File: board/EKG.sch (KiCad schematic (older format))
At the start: 24 parts, among them U1 MAX86150EFF+T

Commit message: worked on schematics: - added new display - delete unwanted parts
Work on PCB:
- cleaned old pcb routes
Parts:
- removed C1, C2: 10pF, Capacitor_SMD:C_0201_0603Metric, symbol Device:C
- removed C3, C7: 22µF, Capacitor_SMD:C_0603_1608Metric, symbol Device:C
- removed C4, C6: 100nF, Capacitor_SMD:C_0201_0603Metric, symbol Device:C
- removed C5, C8: 1µF, Capacitor_SMD:C_0402_1005Metric, symbol Device:C
- removed R1, R2, R3, R8: 0, Resistor_SMD:R_0201_0603Metric, symbol Device:R
- removed R4, R7: DNP, Resistor_SMD:R_0201_0603Metric, symbol Device:R
- removed R5, R6, R9: 49.9k, Resistor_SMD:R_0201_0603Metric, symbol Device:R
- removed TP1: ECG_N, TestPoint:TestPoint_THTPad_D2.0mm_Drill1.0mm, symbol Connector:TestPoint
- removed TP2: ECG_P, TestPoint:TestPoint_THTPad_D2.0mm_Drill1.0mm, symbol Connector:TestPoint
- removed U1: MAX86150EFF+T, maxim:MAX86150, symbol MAX86150:MAX86150EFF+T
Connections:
- no-connect marks 8 -> 0

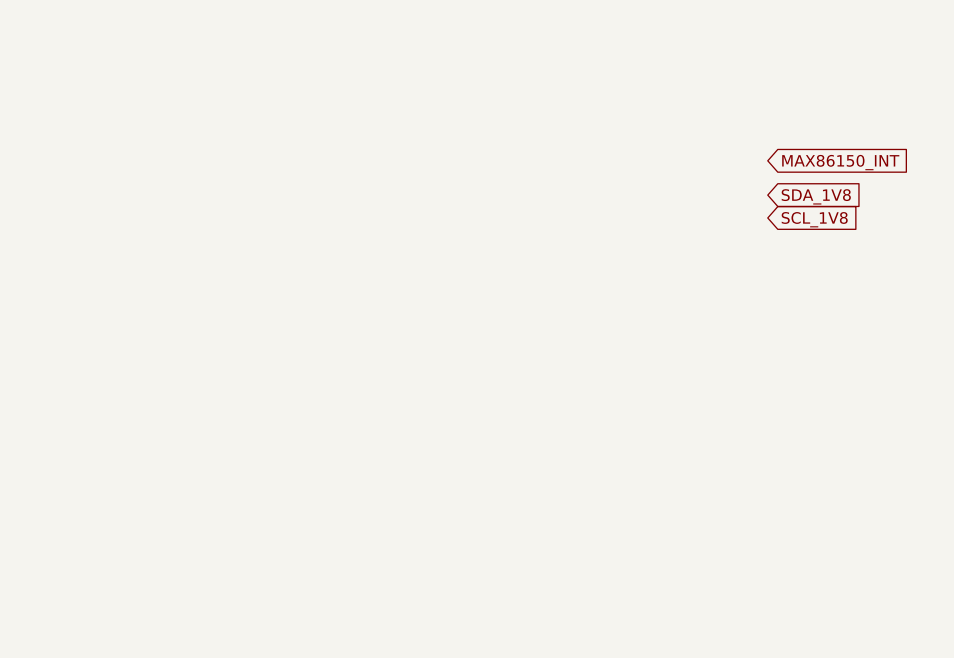
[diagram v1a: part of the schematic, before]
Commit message: - Added connector lib - added footprint for schottkey diode - added keep-out for new display
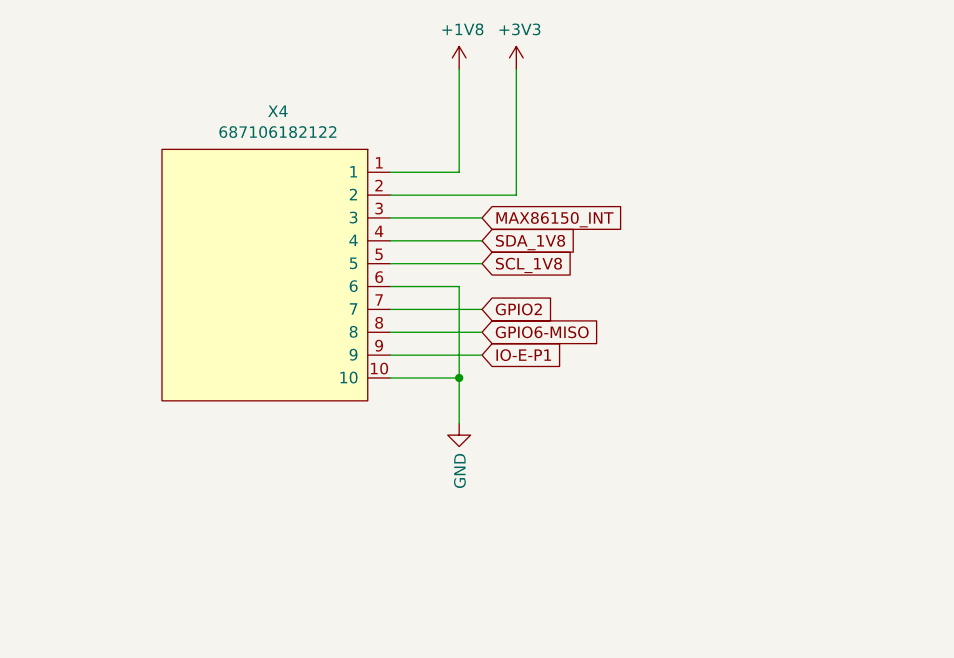
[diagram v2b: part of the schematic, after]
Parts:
- added X4: 687106182122, WR-FPC 0.50 mm SMT ZIF Horizontal Dual Contact:687110182122, symbol 687106182122:687106182122
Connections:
- net MAX86150_INT: now also X4.3
- net SCL_1V8: now also X4.5
- net SDA_1V8: now also X4.4
- new net +1V8: X4.1
- new net +3V3: X4.2
- new net GND: X4.10, X4.6
- new net GPIO2: X4.7
- new net GPIO6-MISO: X4.8
- new net IO-E-P1: X4.9
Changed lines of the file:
@@
 Comment4 ""
 $EndDescr
-Text GLabel 7800 3650 2    50   Input ~ 0
+Text GLabel 6550 3850 2    50   Input ~ 0
 SDA_1V8
-Text GLabel 7800 3750 2    50   Input ~ 0
+Text GLabel 6550 3950 2    50   Input ~ 0
 SCL_1V8
-Text GLabel 7800 3500 2    50   Input ~ 0
+Text GLabel 6550 3750 2    50   Input ~ 0
 MAX86150_INT
 $Comp
@@
 	-1   0    0    1
 $EndComp
+$Comp
+L power:+1V8 #PWR?
+U 1 1 610C6323
+P 6450 3100
+AR Path="/5CB104E6/610C6323" Ref="#PWR?"  Part="1"
+AR Path="/5CB104CE/610C6323" Ref="#PWR0115"  Part="1"
+F 0 "#PWR0115" H 6450 2950 50  0001 C CNN
+F 1 "+1V8" H 6465 3273 50  0000 C CNN
+F 2 "" H 6450 3100 50  0001 C CNN
+F 3 "" H 6450 3100 50  0001 C CNN
+	1    6450 3100
+	1    0    0    -1
+$EndComp
+$Comp
+L power:+3V3 #PWR?
+U 1 1 610C6329
+P 6700 3100
+AR Path="/5CB104E6/610C6329" Ref="#PWR?"  Part="1"
+AR Path="/5CB104CE/610C6329" Ref="#PWR0116"  Part="1"
+F 0 "#PWR0116" H 6700 2950 50  0001 C CNN
+F 1 "+3V3" H 6715 3273 50  0000 C CNN
+F 2 "" H 6700 3100 50  0001 C CNN
+F 3 "" H 6700 3100 50  0001 C CNN
+	1    6700 3100
+	1    0    0    -1
+$EndComp
+$Comp
+L power:GND #PWR?
+U 1 1 610C6FD9
+P 6450 4650
+AR Path="/5CB104E6/610C6FD9" Ref="#PWR?"  Part="1"
+AR Path="/5CB104CE/610C6FD9" Ref="#PWR0117"  Part="1"
+F 0 "#PWR0117" H 6450 4400 50  0001 C CNN
+F 1 "GND" V 6455 4522 50  0000 R CNN
+F 2 "" H 6450 4650 50  0001 C CNN
+F 3 "" H 6450 4650 50  0001 C CNN
+	1    6450 4650
+	1    0    0    -1
+$EndComp
+Text GLabel 6550 4350 2    50   Input ~ 0
+IO-E-P1
+Text GLabel 6550 4250 2    50   Input ~ 0
+GPIO6-MISO
+Text GLabel 6550 4150 2    50   Input ~ 0
+GPIO2
+$Comp
+L 687106182122:687106182122 X4
+U 1 1 610D31AF
+P 5600 4000
+F 0 "X4" H 5658 4715 50  0000 C CNN
+F 1 "687106182122" H 5658 4624 50  0000 C CNN
+F 2 "WR-FPC 0.50 mm SMT ZIF Horizontal Dual Contact:687110182122" H 5900 4550 50  0001 C CNN
+F 3 "" H 5900 4550 50  0001 C CNN
+	1    5600 4000
+	1    0    0    -1
+$EndComp
+Wire Wire Line
+	6450 3550 6150 3550
+Wire Wire Line
+	6450 3100 6450 3550
+Wire Wire Line
+	6700 3650 6150 3650
+Wire Wire Line
+	6700 3100 6700 3650
+Wire Wire Line
+	6450 4650 6450 4450
+Wire Wire Line
+	6450 4450 6150 4450
+Wire Wire Line
+	6150 3750 6550 3750
+Wire Wire Line
+	6550 3850 6150 3850
+Wire Wire Line
+	6150 3950 6550 3950
+Wire Wire Line
+	6150 4150 6550 4150
+Wire Wire Line
+	6550 4250 6150 4250
+Wire Wire Line
+	6150 4350 6550 4350
+Wire Wire Line
+	6450 4450 6450 4050
+Wire Wire Line
+	6450 4050 6150 4050
+Connection ~ 6450 4450
 $EndSCHEMATC
